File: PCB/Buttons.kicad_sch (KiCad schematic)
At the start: 45 parts, among them SW10 MX_SW_HS, SW11 MX_SW_solder, SW12 MX_SW_HS, SW13 MX_SW_solder, SW14 MX_SW_solder, SW15 MX_SW_HS, SW16 MX_SW_HS, SW17 MX_SW_solder, SW18 MX_SW_solder, SW19 MX_SW_HS, SW2 MX_SW_HS, SW20 MX_SW_solder, SW21 MX_SW_HS, SW22 MX_SW_solder, SW23 MX_SW_HS, SW24 MX_SW_HS, SW25 MX_SW_solder, SW26 MX_SW_solder, SW27 MX_SW_HS, SW28 MX_SW_HS, SW29 MX_SW_solder, SW3 MX_SW_solder, SW30 MX_SW_HS, SW31 MX_SW_solder, SW32 MX_SW_HS, SW33 MX_SW_solder, SW34 MX_SW_HS, SW35 MX_SW_solder, SW36 MX_SW_HS, SW37 MX_SW_solder, SW38 MX_SW_solder, SW39 MX_SW_HS, SW4 MX_SW_solder, SW40 MX_SW_solder, SW41 MX_SW_HS, SW42 SW_Push, SW43 SW_Push, SW5 MX_SW_HS, SW6 MX_SW_solder, SW7 MX_SW_HS, SW8 MX_SW_solder, SW9 MX_SW_HS

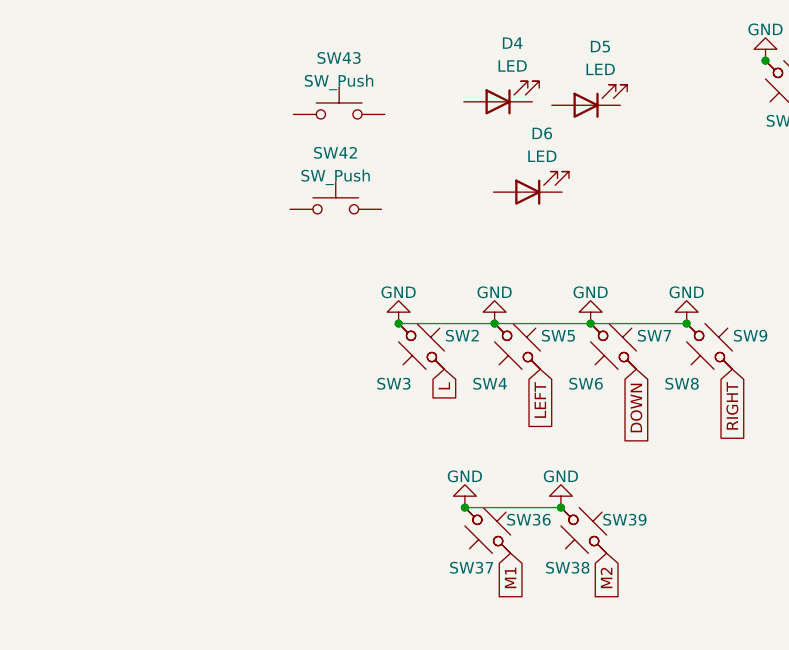
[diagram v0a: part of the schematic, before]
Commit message: Added separated board for the DB
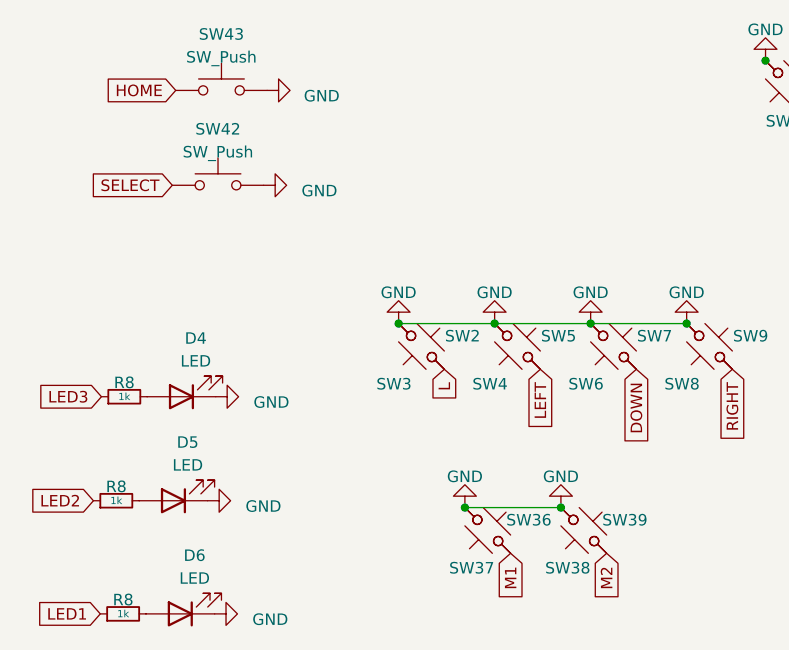
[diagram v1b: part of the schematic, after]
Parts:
- added R8 (x3): 1k, Resistor_SMD:R_0603_1608Metric, symbol Device:R_Small
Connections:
- net GND: now also D4.1 (K), D5.1 (K), D6.1 (K), SW42.1, SW43.1
- net at D5.2 (A): now also R8.2
- net HOME: now reaches SW43.2
- net at D6.2 (A): now also R8.2
- net SELECT: now reaches SW42.2
- net at D4.2 (A): now also R8.2
- new net LED1: R8.1
- new net LED2: R8.1
- new net LED3: R8.1
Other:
- moved on the sheet: D4, D5, D6, SW42, SW43

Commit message: Finished main PCB
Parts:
- removed D4, D5, D6: LED, LED_THT:LED_D3.0mm, symbol Device:LED
- removed R8 (x3): 1k, Resistor_SMD:R_0603_1608Metric, symbol Device:R_Small
- renumbered SW6 to SW10, SW7 to SW11, SW8 to SW12, SW9 to SW13, SW40 to SW14, SW41 to SW15, SW26 to SW16, SW27 to SW17, SW10 to SW18, SW11 to SW19, SW18 to SW20, SW19 to SW21, SW28 to SW22, SW29 to SW23, SW12 to SW24, SW13 to SW25, SW20 to SW26, SW21 to SW27, SW30 to SW28, SW31 to SW29, SW14 to SW30, SW15 to SW31, SW22 to SW32, SW23 to SW33, SW32 to SW34, SW33 to SW35, SW16 to SW36, SW17 to SW37, SW24 to SW38, SW25 to SW39, SW36 to SW4, SW34 to SW40, SW35 to SW41, SW37 to SW5, SW4 to SW6, SW5 to SW7, SW38 to SW8, SW39 to SW9
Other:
- moved on the sheet: SW42, SW43
